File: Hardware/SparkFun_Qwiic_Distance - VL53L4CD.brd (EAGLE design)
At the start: 25.4 x 25.4 mm, 50 parts, among them J2 QWIIC_RIGHT_ANGLE, J4 QWIIC_RIGHT_ANGLE, U1 VL53L4CX

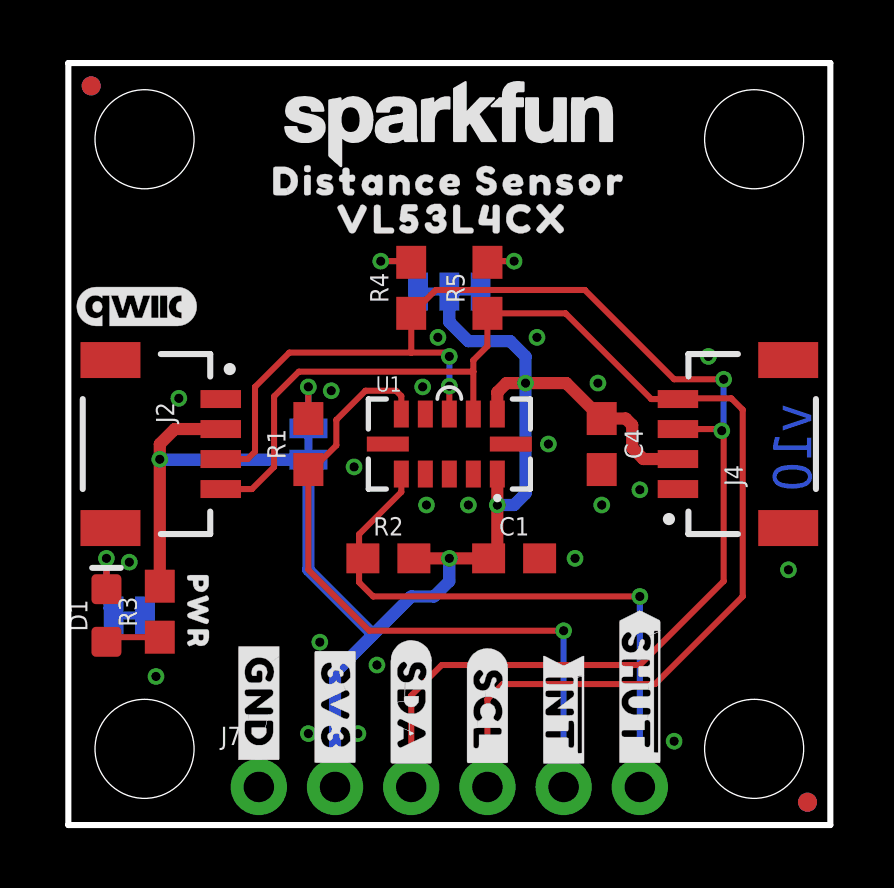
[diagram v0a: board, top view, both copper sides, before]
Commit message: Corrects part name, and changes eagle file names to reflect the change.
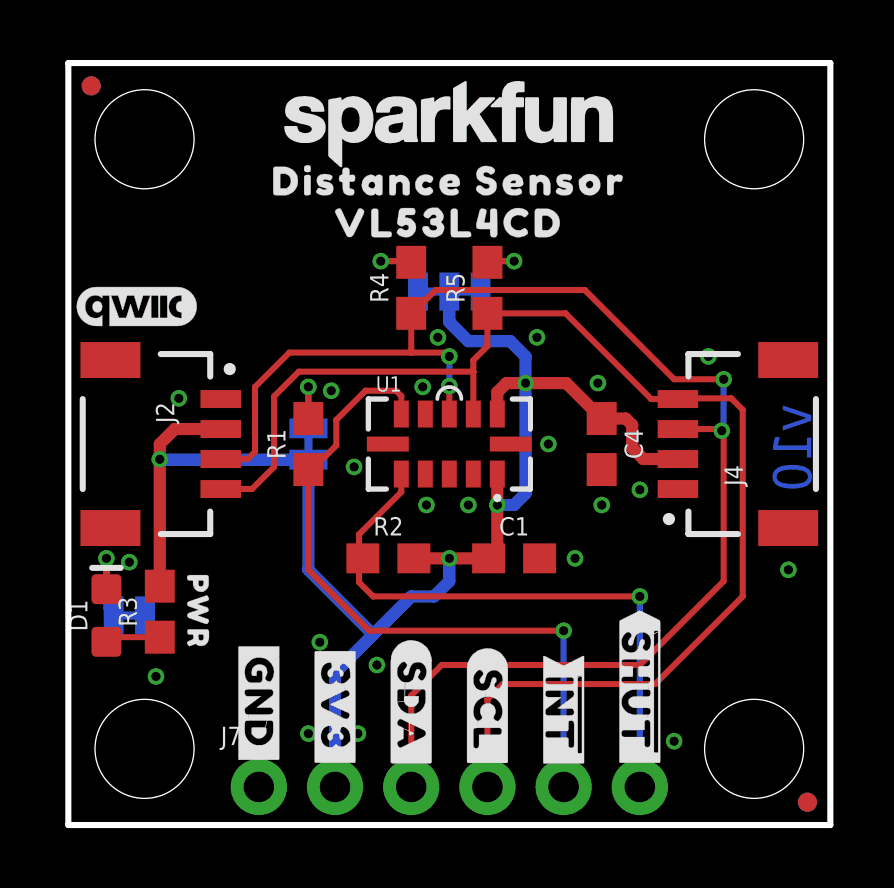
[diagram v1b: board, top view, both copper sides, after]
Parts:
- removed U$19: (no value), distanceSensor:VL53L4CX9
- added U$24: (no value), top:VL53L4CD0
- U$9: device distanceSensor:VL53L4CX9 -> top:VL53L4CD0
- moved U$9 0.18 mm to (12.7, 20.1)
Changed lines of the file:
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@@
 <?xml version="1.0" encoding="utf-8"?>
 <!DOCTYPE eagle SYSTEM "eagle.dtd">
-<eagle version="9.6.2">
+<eagle version="9.5.1">
 <drawing>
 <settings>
@@
 <element name="U$7" library="distanceSensor" package="#SDA#5" value="" x="11.43" y="3.937" smashed="yes" rot="R270"/>
 <element name="U$8" library="distanceSensor" package="DISTANCE_SENSOR8" value="" x="12.7" y="21.463" smashed="yes"/>
-<element name="U$9" library="distanceSensor" package="VL53L4CX9" value="" x="12.827" y="20.193" smashed="yes"/>
 <element name="U$10" library="distanceSensor" package="#LED#54" value="" x="4.572" y="6.985" smashed="yes" rot="MR0"/>
 <element name="U$11" library="distanceSensor" package="#INT#55" value="" x="10.16" y="12.7" smashed="yes" rot="MR0"/>
@@
 <element name="U$17" library="distanceBot" package="#SDA#5" value="" x="11.43" y="3.937" smashed="yes" rot="MR90"/>
 <element name="U$18" library="distanceSensor" package="DISTANCE_SENSOR8" value="" x="12.446" y="24.003" smashed="yes" rot="MR0"/>
-<element name="U$19" library="distanceSensor" package="VL53L4CX9" value="" x="12.7" y="22.606" smashed="yes" rot="MR0"/>
 <element name="U$20" library="distanceSensor" package="DEF_ADDR#54" value="" x="14.224" y="20.955" smashed="yes" rot="MR0"/>
 <element name="U$21" library="distanceSensor" package="0X2955" value="" x="9.652" y="20.955" smashed="yes" rot="MR0"/>
@@
 <element name="U$22" library="SparkFun-Aesthetics" package="SFE_LOGO_FLAME_.1" value="" x="5.588" y="22.479" smashed="yes" rot="MR0"/>
 <element name="U$23" library="distanceSensor" package="PWR55" value="" x="4.318" y="7.112" smashed="yes" rot="R270"/>
+<element name="U$9" library="top" package="VL53L4CD0" value="" x="12.7" y="20.066" smashed="yes"/>
+<element name="U$24" library="top" package="VL53L4CD0" value="" x="12.446" y="22.479" smashed="yes" rot="MR0"/>
 </elements>
 <signals>

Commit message: Updates Distance Sensor Part name
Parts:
- U1: value VL53L4CX -> VL53L4CD; device DISTANCE:VL53L4CX -> DISTANCE:VL53L4CD
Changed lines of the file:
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@@
 <attribute name="REV" value="" x="-16.51" y="-16.51" size="1.778" layer="27" display="off"/>
 </element>
-<element name="U1" library="DISTANCE" package="VL53L4CX" value="VL53L4CX" x="12.7" y="12.7" smashed="yes">
+<element name="U1" library="DISTANCE" package="VL53L4CD" value="VL53L4CD" x="12.7" y="12.7" smashed="yes">
 <attribute name="NAME" x="10.25" y="14.45" size="0.508" layer="25" font="vector"/>
 <attribute name="PROD_ID" value="IC-16332" x="12.7" y="12.7" size="1.778" layer="27" display="off"/>
